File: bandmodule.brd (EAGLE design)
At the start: 35.5 x 41.3 mm, 16 parts

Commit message: Merge C5 and C6 again
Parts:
- removed C6: unused, capacitor-wima:C5B2.5
- renumbered C5 to C5-6
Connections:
- net GND: no longer C6.1
- net N$5: no longer C6.2
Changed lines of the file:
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@@
 <attribute name="NAME" x="10.033" y="10.0965" size="1.27" layer="25" ratio="10"/>
 </element>
-<element name="C5" library="capacitor-wima" package="C5B2.5" value="330p" x="30.1625" y="27.305" smashed="yes" rot="R90">
+<element name="C5-6" library="capacitor-wima" package="C5B2.5" value="330p" x="30.1625" y="27.305" smashed="yes" rot="R90">
 <attribute name="NAME" x="33.0835" y="25.908" size="1.27" layer="25" ratio="10" rot="R90"/>
 </element>
@@
 <attribute name="SPICEPREFIX" value="L" x="17.145" y="15.875" size="1.778" layer="27" display="off"/>
 </element>
-<element name="C6" library="capacitor-wima" package="C5B2.5" value="unused" x="27.305" y="27.305" smashed="yes" rot="R90">
-<attribute name="NAME" x="25.781" y="25.908" size="1.27" layer="25" ratio="10" rot="R90"/>
-</element>
 </elements>
 <signals>
@@
 <contactref element="CT2" pad="1"/>
 <contactref element="C2" pad="2"/>
-<contactref element="C5" pad="1"/>
+<contactref element="C5-6" pad="1"/>
 <contactref element="C12" pad="1"/>
 <contactref element="L4" pad="2"/>
@@
 <vertex x="0" y="0"/>
 </polygon>
-<contactref element="C6" pad="1"/>
 </signal>
 <signal name="N$1">
@@
 <contactref element="L8" pad="P$2"/>
 <contactref element="L7" pad="P$2"/>
-<contactref element="C5" pad="2"/>
+<contactref element="C5-6" pad="2"/>
 <contactref element="C3" pad="2"/>
-<wire x1="30.1625" y1="29.845" x2="30.7975" y2="29.845" width="0.4064" layer="16"/>
+<wire x1="30.7975" y1="29.845" x2="30.1625" y2="29.845" width="0.4064" layer="16"/>
 <wire x1="30.7975" y1="29.845" x2="32.0675" y2="31.115" width="0.4064" layer="16"/>
 <wire x1="32.0675" y1="31.115" x2="32.0675" y2="33.655" width="0.4064" layer="16"/>
-<wire x1="25.3675" y1="31.87" x2="25.3675" y2="29.8775" width="0.4064" layer="16"/>
+<wire x1="25.3675" y1="29.8775" x2="25.3675" y2="31.87" width="0.4064" layer="16"/>
 <wire x1="25.3675" y1="29.8775" x2="25.4" y2="29.845" width="0.4064" layer="16"/>
 <wire x1="25.4" y1="29.845" x2="22.455" y2="29.845" width="0.4064" layer="16"/>
 <wire x1="22.455" y1="29.845" x2="20.835" y2="28.225" width="0.4064" layer="16"/>
-<contactref element="C6" pad="2"/>
-<wire x1="25.3675" y1="29.8775" x2="27.305" y2="29.8775" width="0.4064" layer="16"/>
-<wire x1="27.305" y1="29.8775" x2="27.305" y2="29.845" width="0.4064" layer="16"/>
-<wire x1="27.305" y1="29.845" x2="30.1625" y2="29.845" width="0.4064" layer="16"/>
+<wire x1="30.1625" y1="29.845" x2="25.4" y2="29.845" width="0.4064" layer="16"/>
+<wire x1="25.4" y1="29.845" x2="25.3675" y2="29.8775" width="0.4064" layer="16"/>
 </signal>
 <signal name="N$6">

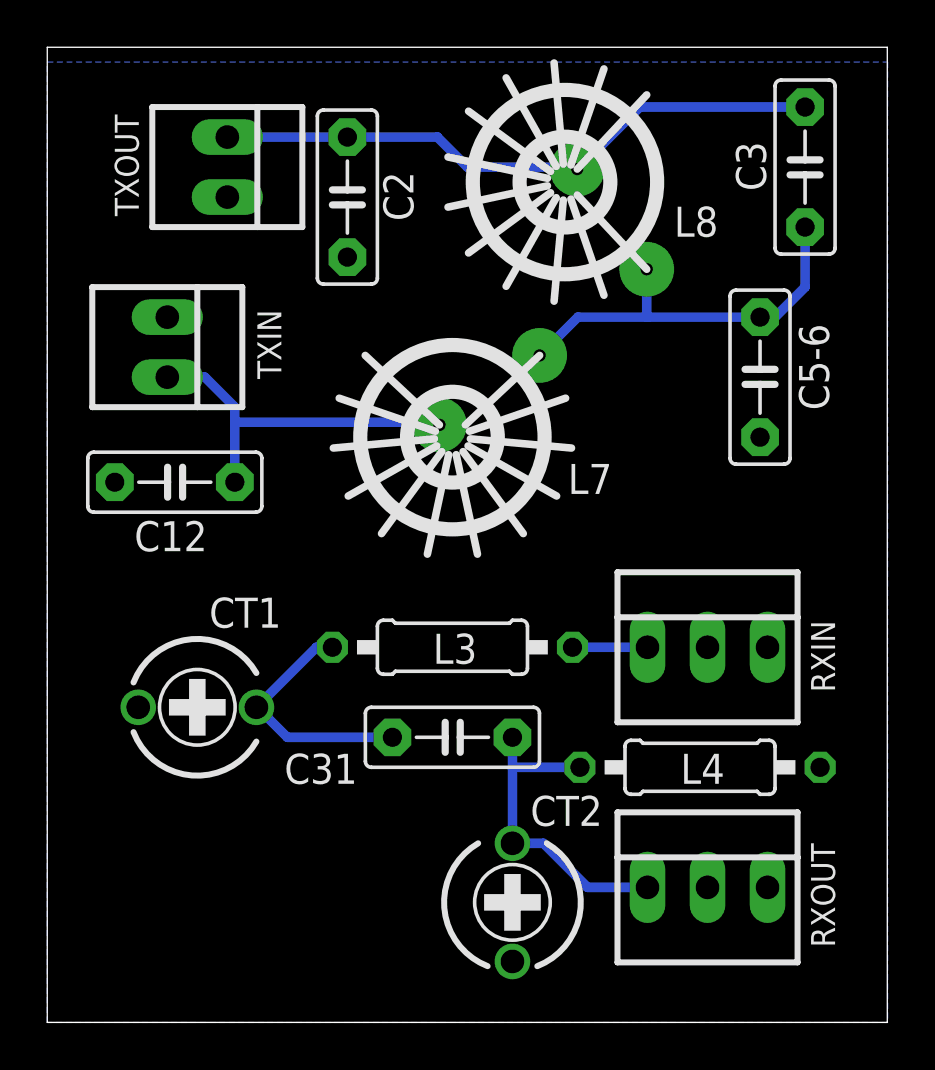
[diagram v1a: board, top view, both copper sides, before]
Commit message: Move L7 and L8 for more space; change artwork
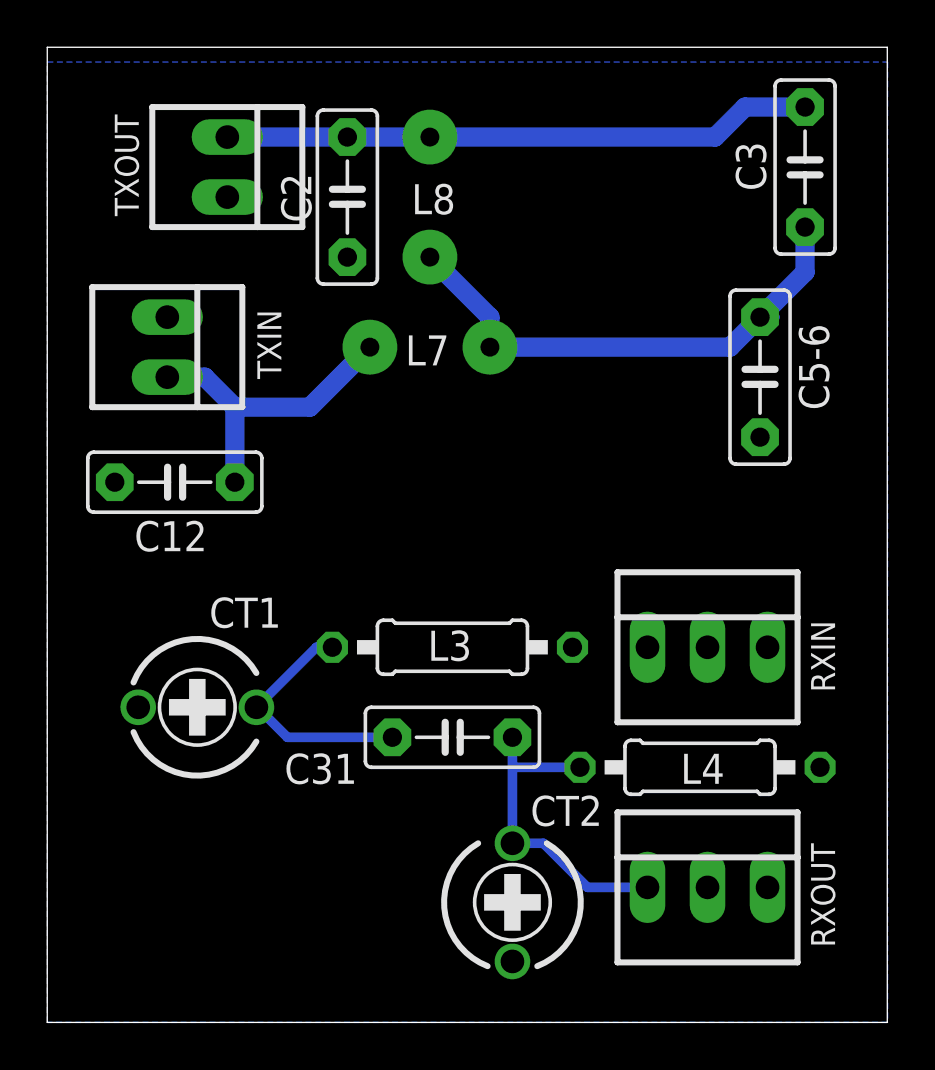
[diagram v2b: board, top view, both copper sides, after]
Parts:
- L7, L8: device toroids:T30-2-28AWG-12T -> toroids:T30-2-28AWG-15T
- moved L8 6.54 mm to (16.2, 32.4)
- moved L7 5.17 mm to (13.7, 28.6), turned to 0 degrees
- turned C2 to 90 degrees
- turned L3 to 180 degrees
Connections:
- net GND: now also C2.1; no longer C2.2
- net N$1: now also L3.1; no longer L3.2
- net N$2: now also L3.2; no longer L3.1
- net N$5: now also L8.P$1; no longer L8.P$2
- net N$8: now also C2.2, L8.P$2; no longer C2.1, L8.P$1
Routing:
- net N$5: track 17.1 -> 22.1 mm
- net N$1: track 3.17 -> 0.00 mm
- net N$6: track 15.4 -> 13.3 mm
- net N$8: track 26.0 -> 25.0 mm
